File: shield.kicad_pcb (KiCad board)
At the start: 4 copper layers, 120 x 120 mm, 109 parts, among them J1 NAPPE_ADC1, J10 OLED_SPI_2x8, J2 NAPPE_ADC2, J3 NAPPE_PWM, J4 NAPPE_GPIO, J5 DEVKIT_C2000_ROW_A, J6 DEVKIT_C2000_ROW_B, J7 ESP32_C6_DEVKITC_1_J1, J8 ESP32_C6_DEVKITC_1_J3, J9 J_PWR_11-25V, U1 LDO_3V3_ISO, U2 NCM3S1205MC, U3 NCM3S1205MC, U4 ER-OLEDM032-1

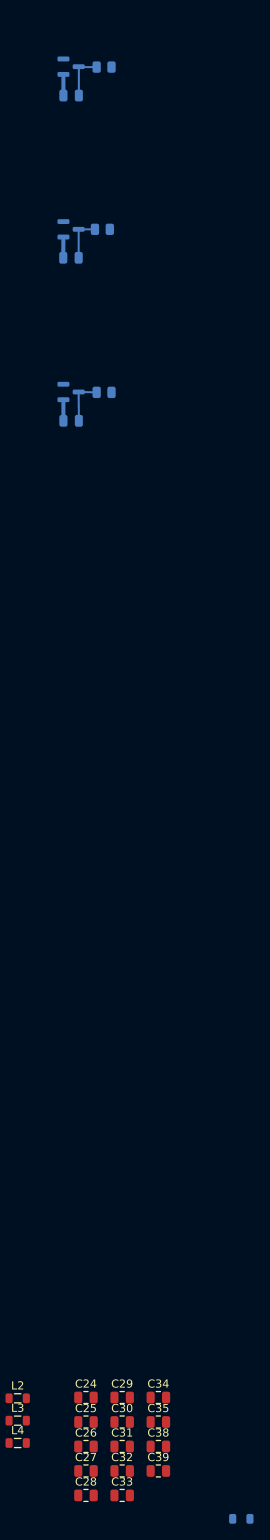
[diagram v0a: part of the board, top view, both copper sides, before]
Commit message: Routage des 23 trios de protection (PCB)
Checkpoint avant le travail de routage des nappes J1-J4 et l'ajout de
J5/J6 (connecteurs de sortie vers les cartes filles).
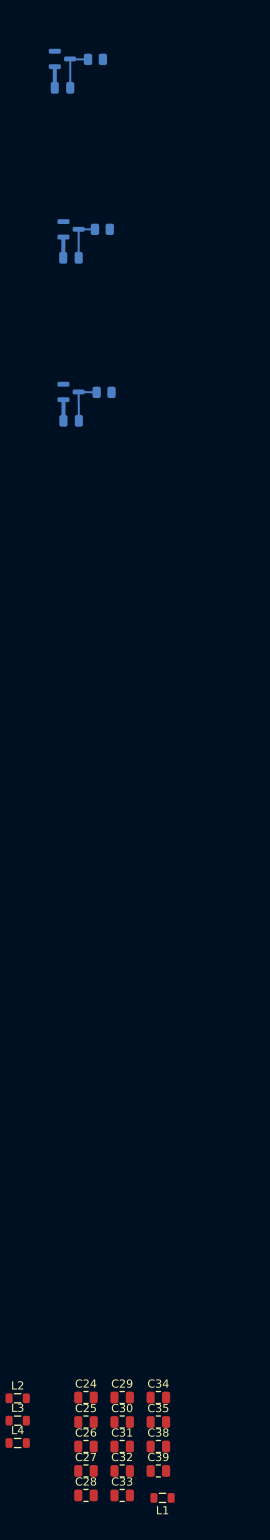
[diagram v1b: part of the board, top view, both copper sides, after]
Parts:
- L1: moved to F.Cu
- moved L1 10.0 mm to (263.2, 261.0), turned to 180 degrees
- moved C3 1.43 mm to (250.9, 87.6)
- moved D4 1.43 mm to (250.9, 84.0)
- moved R3 1.43 mm to (255.0, 84.1)
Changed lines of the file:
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@@
 		)
 	)
+	(footprint "Inductor_SMD:L_0805_2012Metric"
+		(layer "F.Cu")
+		(at 263.25 261 180)
+		(descr "Inductor SMD 0805 (2012 Metric), square (rectangular) end terminal, IPC-7351 nominal, (Body size source: IPC-SM-782 page 80, https://www.pcb-3d.com/wordpress/wp-content/uploads/ipc-sm-782a_amendment_1_and_2.pdf)")
+		(tags "inductor")
+		(property "Reference" "L1"
+			(at 0 -1.55 0)
+			(layer "F.SilkS")
+			(effects
+				(font
+					(size 1 1)
+					(thickness 0.15)
+				)
+			)
+		)
+		(property "Value" "22uH"
+			(at 0 1.55 0)
+			(layer "F.Fab")
+			(effects
+				(font
+					(size 1 1)
+					(thickness 0.15)
+				)
+			)
+		)
+		(property "Datasheet" ""
+			(at 0 0 0)
+			(layer "F.Fab")
+			(hide yes)
+			(effects
+				(font
+					(size 1.27 1.27)
+				)
+			)
+		)
+		(property "Description" ""
+			(at 0 0 0)
+			(layer "F.Fab")
+			(hide yes)
+			(effects
+				(font
+					(size 1.27 1.27)
+				)
+			)
+		)
+		(property "KiLib_Generator" "SMD_2terminal_chip_molded"
+			(at 0 0 0)
+			(layer "F.SilkS")
+			(hide yes)
+			(effects
+				(font
+					(size 1 1)
+					(thickness 0.15)
+				)
+			)
+		)
+		(property ki_fp_filters "Choke_* *Coil* Inductor_* L_*")
+		(sheetname "/DC/")
+		(sheetfile "dc.kicad_sch")
+		(attr smd)
+		(duplicate_pad_numbers_are_jumpers no)
+		(fp_line
+			(start -0.399622 0.56)
+			(end 0.399622 0.56)
+			(stroke
+				(width 0.12)
+				(type solid)
+			)
+			(layer "F.SilkS")
+		)
+		(fp_line
+			(start -0.399622 -0.56)
+			(end 0.399622 -0.56)
+			(stroke
+				(width 0.12)
+				(type solid)
+			)
+			(layer "F.SilkS")
+		)
+		(fp_rect
+			(start -1.75 0.85)
+			(end 1.75 -0.85)
+			(stroke
+				(width 0.05)
+				(type solid)
+			)
+			(fill no)
+			(layer "F.CrtYd")
+		)
+		(fp_rect
+			(start -1 0.45)
+			(end 1 -0.45)
+			(stroke
+				(width 0.1)
+				(type solid)
+			)
+			(fill no)
+			(layer "F.Fab")
+		)
+		(fp_text user "${REFERENCE}"
+			(at 0 0 0)
+			(layer "F.Fab")
+			(effects
+				(font
+					(size 0.5 0.5)
+					(thickness 0.08)
+				)
+			)
+		)
+		(pad "1" smd roundrect
+			(at -1.0625 0 180)
+			(size 0.875 1.2)
+			(layers "F.Cu" "F.Mask" "F.Paste")
+			(roundrect_rratio 0.25)
+			(net "VIN_PWR")
+			(pinfunction "1_1")
+			(pintype "passive")
+		)
+		(pad "2" smd roundrect
+			(at 1.0625 0 180)
+			(size 0.875 1.2)
+			(layers "F.Cu" "F.Mask" "F.Paste")
+			(roundrect_rratio 0.25)
+			(net "U2_VINF")
+			(pinfunction "2_2")
+			(pintype "passive")
+		)
+		(embedded_fonts no)
+		(model "${KICAD10_3DMODEL_DIR}/Inductor_SMD.3dshapes/L_0805_2012Metric.step"
+			(offset
+				(xyz 0 0 0)
+			)
+			(scale
+				(xyz 1 1 1)
+			)
+			(rotate
+				(xyz 0 0 0)
+			)
+		)
+	)
 	(footprint "Capacitor_SMD:C_0805_2012Metric"
 		(layer "F.Cu")
@@
 	(footprint "Capacitor_SMD:C_0805_2012Metric"
 		(layer "B.Cu")
-		(at 252.0125 88.55)
+		(at 250.95 87.6)
 		(descr "Capacitor SMD 0805 (2012 Metric), square (rectangular) end terminal, IPC-7351 nominal, (Body size source: IPC-SM-782 page 76, https://www.pcb-3d.com/wordpress/wp-content/uploads/ipc-sm-782a_amendment_1_and_2.pdf, https://docs.google.com/spreadsheets/d/1BsfQQcO9C6DZCsRaXUlFlo91Tg2WpOkGARC1WS5S8t0/edit?usp=sharing)")
 		(tags "capacitor")
@@
 		(embedded_fonts no)
 	)
-	(footprint "Inductor_SMD:L_0805_2012Metric"
-		(layer "B.Cu")
-		(at 272.9375 263.575)
-		(descr "Inductor SMD 0805 (2012 Metric), square (rectangular) end terminal, IPC-7351 nominal, (Body size source: IPC-SM-782 page 80, https://www.pcb-3d.com/wordpress/wp-content/uploads/ipc-sm-782a_amendment_1_and_2.pdf)")
-		(tags "inductor")
-		(property "Reference" "L1"
-			(at 0 1.55 0)
-			(layer "B.SilkS")
-			(effects
-				(font
-					(size 1 1)
-					(thickness 0.15)
-				)
-				(justify mirror)
-			)
-		)
-		(property "Value" "22uH"
-			(at 0 -1.55 0)
-			(layer "B.Fab")
-			(effects
-				(font
-					(size 1 1)
-					(thickness 0.15)
-				)
-				(justify mirror)
-			)
-		)
-		(property "Datasheet" ""
-			(at 0 0 0)
-			(layer "B.Fab")
-			(hide yes)
-			(effects
-				(font
-					(size 1.27 1.27)
-				)
-				(justify mirror)
-			)
-		)
-		(property "Description" ""
-			(at 0 0 0)
-			(layer "B.Fab")
-			(hide yes)
-			(effects
-				(font
-					(size 1.27 1.27)
-				)
-				(justify mirror)
-			)
-		)
-		(property "KiLib_Generator" "SMD_2terminal_chip_molded"
-			(at 0 0 0)
-			(layer "B.SilkS")
-			(hide yes)
-			(effects
-				(font
-					(size 1 1)
-					(thickness 0.15)
-				)
-				(justify mirror)
-			)
-		)
-		(property ki_fp_filters "Choke_* *Coil* Inductor_* L_*")
-		(sheetname "/DC/")
-		(sheetfile "dc.kicad_sch")
-		(attr smd)
-		(duplicate_pad_numbers_are_jumpers no)
-		(fp_line
-			(start -0.399622 -0.56)
-			(end 0.399622 -0.56)
-			(stroke
-				(width 0.12)
-				(type solid)
-			)
-			(layer "B.SilkS")
-		)
-		(fp_line
-			(start -0.399622 0.56)
-			(end 0.399622 0.56)
-			(stroke
-				(width 0.12)
-				(type solid)
-			)
-			(layer "B.SilkS")
-		)
-		(fp_rect
-			(start -1.75 -0.85)
-			(end 1.75 0.85)
-			(stroke
-				(width 0.05)
-				(type solid)
-			)
-			(fill no)
-			(layer "B.CrtYd")
-		)
-		(fp_rect
-			(start -1 -0.45)
-			(end 1 0.45)
-			(stroke
-				(width 0.1)
-				(type solid)
-			)
-			(fill no)
-			(layer "B.Fab")
-		)
-		(fp_text user "${REFERENCE}"
-			(at 0 0 0)
-			(layer "B.Fab")
-			(effects
-				(font
-					(size 0.5 0.5)
-					(thickness 0.08)
-				)
-				(justify mirror)
-			)
-		)
-		(pad "1" smd roundrect
-			(at -1.0625 0)
-			(size 0.875 1.2)
-			(layers "B.Cu" "B.Mask" "B.Paste")
-			(roundrect_rratio 0.25)
-			(net "VIN_PWR")
-			(pinfunction "1_1")
-			(pintype "passive")
-		)
-		(pad "2" smd roundrect
-			(at 1.0625 0)
-			(size 0.875 1.2)
-			(layers "B.Cu" "B.Mask" "B.Paste")
-			(roundrect_rratio 0.25)
-			(net "U2_VINF")
-			(pinfunction "2_2")
-			(pintype "passive")
-		)
-		(embedded_fonts no)
-		(model "${KICAD10_3DMODEL_DIR}/Inductor_SMD.3dshapes/L_0805_2012Metric.step"
-			(offset
-				(xyz 0 0 0)
-			)
-			(scale
-				(xyz 1 1 1)
-			)
-			(rotate
-				(xyz 0 0 0)
-			)
-		)
-	)
 	(footprint "Resistor_SMD:R_0805_2012Metric"
 		(layer "B.Cu")
@@
 	(footprint "Package_TO_SOT_SMD:SOT-23"
 		(layer "B.Cu")
-		(at 252 85)
+		(at 250.9375 84.05)
 		(descr "SOT, 3 Pin (JEDEC TO-236 Var AB https://www.jedec.org/document_search?search_api_views_fulltext=TO-236)")
 		(tags "SOT TO_SOT_SMD")
@@
 	(footprint "Resistor_SMD:R_0805_2012Metric"
 		(layer "B.Cu")
-		(at 256.0625 85.05 180)
+		(at 255 84.1 180)
 		(descr "Resistor SMD 0805 (2012 Metric), square (rectangular) end terminal, IPC-7351 nominal, (Body size source: IPC-SM-782 page 72, https://www.pcb-3d.com/wordpress/wp-content/uploads/ipc-sm-782a_amendment_1_and_2.pdf)")
 		(tags "resistor")
@@
 	)
 	(segment
-		(start 251.0625 85.95)
-		(end 251.0625 88.55)
+		(start 250 85)
+		(end 250 87.6)
 		(width 0.5)
 		(layer "B.Cu")
@@
 	)
 	(segment
-		(start 255.15 85.05)
-		(end 252.9875 85.05)
+		(start 254.0875 84.1)
+		(end 251.925 84.1)
 		(width 0.25)
 		(layer "B.Cu")
@@
 	)
 	(segment
-		(start 252.9625 88.55)
-		(end 252.9625 85.025)
+		(start 251.9 87.6)
+		(end 251.9 84.075)
 		(width 0.25)
 		(layer "B.Cu")
@@
 	)
 	(segment
-		(start 252.9625 85.025)
-		(end 252.9375 85)
+		(start 251.9 84.075)
+		(end 251.875 84.05)
 		(width 0.25)
 		(layer "B.Cu")
@@
 	)
 	(segment
-		(start 252.9875 85.05)
-		(end 252.9625 85.025)
+		(start 251.925 84.1)
+		(end 251.9 84.075)
 		(width 0.25)
 		(layer "B.Cu")

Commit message: Decouplage 100nF sur les 6 nappes (3V3_ISO/GND)
Un condensateur par connecteur (C29, C30, C34, C35, C42, C43), au plus
pres de chaque embase - complement du decouplage par IC deja en place,
pour que chaque nappe ait sa propre reserve locale avant la traversee du
cable. Place manuellement par l'utilisateur dans l'editeur KiCad.
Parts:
- added C42: 100nF, Capacitor_SMD:C_0805_2012Metric, B.Cu at (226.7, 77.8)
- added C43: 100nF, Capacitor_SMD:C_0805_2012Metric, B.Cu at (226.8, 119.2)
- added J13: NAPPE_GPIO2, Connector_IDC:IDC-Header_2x10_P2.54mm_Vertical, F.Cu at (250.5, 121.5)
- added J14: NAPPE_COM, Connector_IDC:IDC-Header_2x10_P2.54mm_Vertical, F.Cu at (250.2, 80.3)
- C29, C30, C34, C35: value 470pF -> 100nF; moved to B.Cu
- J4: value NAPPE_GPIO -> NAPPE_GPIO1
- moved C35 185.0 mm to (198.9, 78.0)
- moved C29 170.8 mm to (251.6, 78.0)
- moved C18 157.3 mm to (213.3, 152.2)
- moved D19 157.3 mm to (213.3, 148.7)
- moved R18 157.3 mm to (217.3, 148.8)
- moved R17 151.7 mm to (218.5, 158.5)
- moved C17 151.7 mm to (214.4, 162.0)
- moved D18 151.7 mm to (214.4, 158.4)
- moved D21 150.6 mm to (226.5, 158.4)
- moved R20 150.6 mm to (230.6, 158.5)
- moved C20 150.6 mm to (226.5, 162.0)
- moved C34 144.0 mm to (198.9, 119.5)
- moved C30 133.1 mm to (251.8, 118.8)
- moved C1 110.0 mm to (184.8, 85.0)
- moved D3 110.0 mm to (184.8, 81.5)
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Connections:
- C29 pad 1: 5V_ISO -> 3V3_ISO
- C30 pad 1: 5V_ISO -> 3V3_ISO
- C34 pad 1: 5V_NUM -> 3V3_ISO
- C35 pad 1: 5V_NUM -> 3V3_ISO
- J1 pad 10: unconnected-(J1-Temp1-Pad10) -> GND
- J1 pad 11: GND -> Temp2
- J1 pad 12: unconnected-(J1-Temp2-Pad12) -> GND
- J1 pad 13: GND -> Iin
- J1 pad 14: unconnected-(J1-Iin-Pad14) -> GND
- J1 pad 15: GND -> Iout
- J1 pad 16: unconnected-(J1-Iout-Pad16) -> GND
- J1 pad 17: GND -> unconnected-(J1-RESERVE_ADC1_1-Pad17)
- J1 pad 18: unconnected-(J1-RESERVE_1-Pad18) -> GND
- J1 pad 19: (no net) -> unconnected-(J1-RESERVE_ADC1_2-Pad19)
- J1 pad 20: (no net) -> GND
- J1 pad 3: GND -> Vin
- J1 pad 4: unconnected-(J1-Vin-Pad4) -> GND
- J1 pad 5: GND -> Vout
- J1 pad 6: unconnected-(J1-Vout-Pad6) -> GND
- J1 pad 7: GND -> V1
- J1 pad 8: unconnected-(J1-V1-Pad8) -> GND
- J1 pad 9: GND -> Temp1
- J2 pad 10: unconnected-(J2-GND-Pad10) -> GND
- J2 pad 11: GND -> unconnected-(J2-RESERVE_ADC2_2-Pad11)
- J2 pad 12: unconnected-(J2-RESERVE_2-Pad12) -> GND
- J2 pad 13: GND -> unconnected-(J2-RESERVE_ADC2_3-Pad13)
- J2 pad 14: unconnected-(J2-RESERVE_3-Pad14) -> GND
- J2 pad 15: GND -> unconnected-(J2-RESERVE_ADC2_4-Pad15)
- J2 pad 16: unconnected-(J2-RESERVE_4-Pad16) -> GND
- J2 pad 17: GND -> unconnected-(J2-RESERVE_ADC2_5-Pad17)
- J2 pad 18: unconnected-(J2-RESERVE_5-Pad18) -> GND
- J2 pad 19: (no net) -> unconnected-(J2-RESERVE_ADC2_6-Pad19)
- J2 pad 20: (no net) -> GND
- J2 pad 3: GND -> I_shunt1
- J2 pad 4: unconnected-(J2-I_shunt1-Pad4) -> GND
- J2 pad 5: GND -> I_shunt2
- J2 pad 6: unconnected-(J2-I_shunt2-Pad6) -> GND
- J2 pad 7: GND -> VREF_ADC
- J2 pad 8: unconnected-(J2-VREF_ADC-Pad8) -> VREFLO_SENSE
- J2 pad 9: GND -> unconnected-(J2-RESERVE_ADC2_1-Pad9)
- J3 pad 10: unconnected-(J3-PWM2_B-Pad10) -> GND
- J3 pad 11: GND -> PWM3_A
- J3 pad 12: unconnected-(J3-PWM3_A-Pad12) -> GND
- J3 pad 13: GND -> PWM3_B
- J3 pad 14: unconnected-(J3-PWM3_B-Pad14) -> GND
- J3 pad 15: GND -> PWM4_A
- J3 pad 16: unconnected-(J3-PWM4_A-Pad16) -> GND
- J3 pad 17: GND -> PWM4_B
- J3 pad 18: unconnected-(J3-PWM4_B-Pad18) -> GND
- J3 pad 19: (no net) -> unconnected-(J3-RESERVE_PWM_1-Pad19)
- J3 pad 20: (no net) -> GND
- J3 pad 3: GND -> PWM1_A
- J3 pad 4: unconnected-(J3-PWM1_A-Pad4) -> GND
- J3 pad 5: GND -> PWM1_B
- J3 pad 6: unconnected-(J3-PWM1_B-Pad6) -> GND
- J3 pad 7: GND -> PWM2_A
- J3 pad 8: unconnected-(J3-PWM2_A-Pad8) -> GND
- J3 pad 9: GND -> PWM2_B
- J4 pad 10: unconnected-(J4-Discharge-Pad10) -> GND
- J4 pad 11: GND -> CMP_OUT
- J4 pad 12: unconnected-(J4-CMP_OUT-Pad12) -> GND
- J4 pad 13: GND -> nFAULT
- J4 pad 14: unconnected-(J4-nFAULT-Pad14) -> GND
- J4 pad 15: GND -> I2C_SCL
- J4 pad 16: unconnected-(J4-I2C_SCL-Pad16) -> GND
- J4 pad 17: GND -> I2C_SDA
- J4 pad 18: unconnected-(J4-I2C_SDA-Pad18) -> GND
- J4 pad 19: (no net) -> CLB_OUT
- J4 pad 20: (no net) -> GND
- J4 pad 3: GND -> Stage1_EN
- J4 pad 4: unconnected-(J4-Stage1_EN-Pad4) -> GND
- J4 pad 5: GND -> Stage2_EN
- J4 pad 6: unconnected-(J4-Stage2_EN-Pad6) -> GND
- J4 pad 7: GND -> HV_EN
- J4 pad 8: unconnected-(J4-HV_EN-Pad8) -> GND
- J4 pad 9: GND -> Discharge
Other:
- board size 120 x 120 mm -> 150 x 120 mm

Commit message: Placement PCB des 11 trios de protection nappe (Phase B, decision #19)
Ajoute, miroir B.Cu et groupe les 11 trios BAT54S+R+C crees en
Phase A (D25-D35/R24-R34/C44-C54), places pres de leurs connecteurs
respectifs (ADC-2, GPIO-1, COM) a l'interieur du contour reel de la
carte. DRC final : 0 copper_edge_clearance, aucune nouvelle
violation imputable aux nouveaux designateurs (courtyards_overlap,
clearance, shorting_items, npth_inside_courtyard verifies
pre-existants par grep).
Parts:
- added C44: 100pF, Capacitor_SMD:C_0805_2012Metric, B.Cu at (239.7, 115.7)
- added C45: 100pF, Capacitor_SMD:C_0805_2012Metric, B.Cu at (239.2, 77.7)
- added C46: 100pF, Capacitor_SMD:C_0805_2012Metric, B.Cu at (164.4, 136.1)
- added C47: 100pF, Capacitor_SMD:C_0805_2012Metric, B.Cu at (118.3, 152.3)
- added C48: 100pF, Capacitor_SMD:C_0805_2012Metric, B.Cu at (126.3, 146.3)
- added C49: 100pF, Capacitor_SMD:C_0805_2012Metric, B.Cu at (114.3, 54.3)
- added C50: 100pF, Capacitor_SMD:C_0805_2012Metric, B.Cu at (116.3, 142.3)
- added C51: 100pF, Capacitor_SMD:C_0805_2012Metric, B.Cu at (114.3, 44.3)
- added C52: 100pF, Capacitor_SMD:C_0805_2012Metric, B.Cu at (126.3, 136.3)
- added C53: 100pF, Capacitor_SMD:C_0805_2012Metric, B.Cu at (134.3, 152.3)
- added C54: 100pF, Capacitor_SMD:C_0805_2012Metric, B.Cu at (124.3, 56.3)
- added D25: BAT54S, Package_TO_SOT_SMD:SOT-23, B.Cu at (239.7, 112.2)
- added D26: BAT54S, Package_TO_SOT_SMD:SOT-23, B.Cu at (239.2, 74.1)
- added D27: BAT54S, Package_TO_SOT_SMD:SOT-23, B.Cu at (164.4, 132.6)
- added D28: BAT54S, Package_TO_SOT_SMD:SOT-23, B.Cu at (118.2, 148.8)
- added D29: BAT54S, Package_TO_SOT_SMD:SOT-23, B.Cu at (126.2, 142.8)
- added D30: BAT54S, Package_TO_SOT_SMD:SOT-23, B.Cu at (114.2, 50.8)
- added D31: BAT54S, Package_TO_SOT_SMD:SOT-23, B.Cu at (116.2, 138.8)
- added D32: BAT54S, Package_TO_SOT_SMD:SOT-23, B.Cu at (114.2, 40.8)
- added D33: BAT54S, Package_TO_SOT_SMD:SOT-23, B.Cu at (126.2, 132.8)
- added D34: BAT54S, Package_TO_SOT_SMD:SOT-23, B.Cu at (134.2, 148.8)
- added D35: BAT54S, Package_TO_SOT_SMD:SOT-23, B.Cu at (124.2, 52.8)
- added R24: 22R, Resistor_SMD:R_0805_2012Metric, B.Cu at (243.8, 112.2)
- added R25: 22R, Resistor_SMD:R_0805_2012Metric, B.Cu at (243.2, 74.2)
- added R26: 100R, Resistor_SMD:R_0805_2012Metric, B.Cu at (168.5, 132.6)
- added R27: 100R, Resistor_SMD:R_0805_2012Metric, B.Cu at (122.3, 148.8)
- added R28: 100R, Resistor_SMD:R_0805_2012Metric, B.Cu at (130.3, 142.8)
- added R29: 100R, Resistor_SMD:R_0805_2012Metric, B.Cu at (118.3, 50.8)
- added R30: 100R, Resistor_SMD:R_0805_2012Metric, B.Cu at (120.3, 138.8)
- added R31: 100R, Resistor_SMD:R_0805_2012Metric, B.Cu at (118.3, 40.8)
- added R32: 100R, Resistor_SMD:R_0805_2012Metric, B.Cu at (130.3, 132.8)
- added R33: 100R, Resistor_SMD:R_0805_2012Metric, B.Cu at (138.3, 148.8)
- added R34: 100R, Resistor_SMD:R_0805_2012Metric, B.Cu at (128.3, 52.8)
- moved C24 247.9 mm to (79.8, 72.2)
- moved C25 247.9 mm to (79.8, 75.2)
- moved C26 247.9 mm to (79.8, 78.2)
- moved C27 247.9 mm to (79.8, 81.2)
- moved C28 247.9 mm to (79.8, 84.3)
- moved C31 247.9 mm to (84.2, 78.2)
- moved C32 247.9 mm to (84.2, 81.2)
- moved C33 247.9 mm to (84.2, 84.3)
- moved C38 247.9 mm to (88.7, 78.2)
- moved C39 247.9 mm to (88.7, 81.2)
- moved L1 247.9 mm to (89.2, 84.6)
- moved L2 247.9 mm to (71.4, 72.3)
- moved L3 247.9 mm to (71.4, 75.1)
- moved L4 247.9 mm to (71.4, 77.8)
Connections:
- J2 pad 11: unconnected-(J2-RESERVE_ADC2_2-Pad11) -> I_SHUNT2_CMP
- J2 pad 9: unconnected-(J2-RESERVE_ADC2_1-Pad9) -> I_SHUNT1_CMP
- J6 pad 15: UART_TX -> UART_TX_MCU
- J6 pad 16: UART_RX -> UART_RX_MCU
- J6 pad 19: SPI_CLK -> SPI_CLK_MCU
- J6 pad 20: SPI_SIMO -> SPI_SIMO_MCU
- J6 pad 21: SPI_SOMI -> SPI_SOMI_MCU
- J6 pad 22: SPI_STE -> SPI_STE_MCU
- J6 pad 24: CAN_TX -> CAN_TX_MCU
- J6 pad 25: CAN_RX -> CAN_RX_MCU
- J6 pad 27: CLB_OUT -> CLB_OUT_MCU

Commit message: Route les connexions internes des 11 trios de protection nappe
Ajoute les 3 pistes par trio (1 GND, 2 signal _MCU) reliant D/R/C
entre eux, meme motif que les trios existants (ex. D3/R1/C1).
Pistes integrees aux groupes PROT_*_MCU deja crees. DRC :
unconnected_items 324->291 (-33, exactement les 11x3 connexions
routees), aucune autre categorie affectee.
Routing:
- net GND: track 59.7 -> 88.3 mm
- net UART_RX_MCU: track 0.00 -> 5.76 mm
- net SPI_STE_MCU: track 0.00 -> 5.76 mm
- net CAN_TX_MCU: track 0.00 -> 5.76 mm
- net UART_TX_MCU: track 0.00 -> 5.76 mm
- net SPI_SIMO_MCU: track 0.00 -> 5.76 mm
- net I_SHUNT2_CMP_MCU: track 0.00 -> 5.76 mm
- net SPI_SOMI_MCU: track 0.00 -> 5.76 mm
- net SPI_CLK_MCU: track 0.00 -> 5.76 mm
- net CAN_RX_MCU: track 0.00 -> 5.76 mm
- net CLB_OUT_MCU: track 0.00 -> 5.76 mm
- net I_SHUNT1_CMP_MCU: track 0.00 -> 5.76 mm
